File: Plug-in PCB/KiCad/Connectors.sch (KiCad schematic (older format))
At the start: 6 parts, among them J2 Conn_01x01, J3 Conn_01x01, J4 Conn_01x01, J5 Conn_01x01, J6 Conn_01x01, J7 Conn_01x01

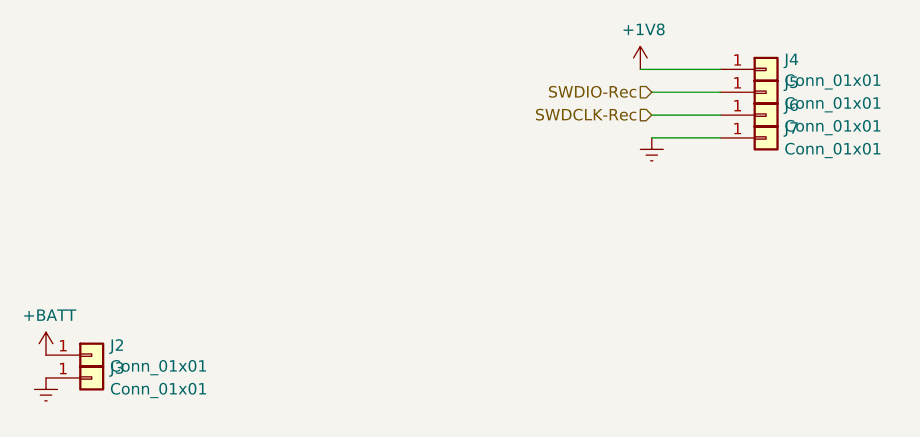
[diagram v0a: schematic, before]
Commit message: Wired Expansion Board Updates
1. KiCad: Schematics and layouts completed/Gerber files generated
2. Atmel: Communication protocol from WireFree to WiredExpansion written
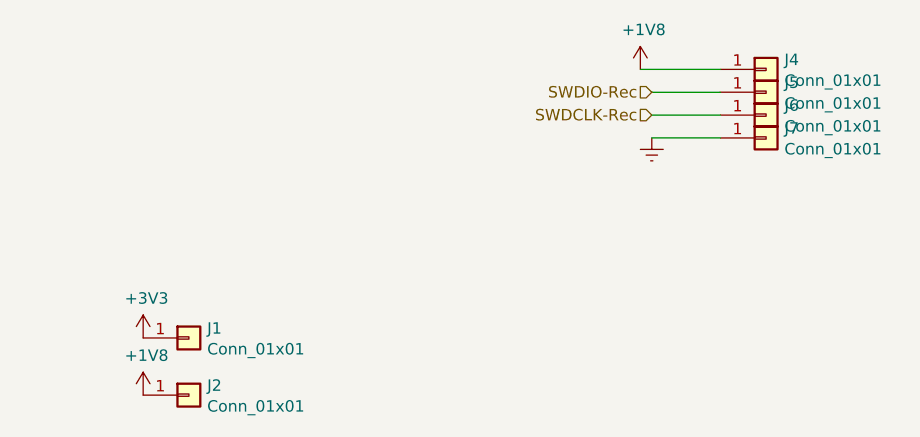
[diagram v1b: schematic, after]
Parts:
- removed J3: Conn_01x01, Connector_PinHeader_2.54mm:PinHeader_1x01_P2.54mm_Vertical, symbol .Connector:Conn_01x01
- added J1: Conn_01x01, Connector_PinHeader_2.54mm:PinHeader_1x01_P2.54mm_Vertical, symbol .Connector:Conn_01x01
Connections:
- net +BATT is gone; now on net +1V8: J2.1 (Pin_1)
- new net +3V3: J1.1 (Pin_1)
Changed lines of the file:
@@
 $EndDescr
-$Comp
-L .Connector:Conn_01x01 J2
-U 1 1 5CA26767
-P 4450 4100
-F 0 "J2" H 4530 4142 50  0000 L CNN
-F 1 "Conn_01x01" H 4530 4051 50  0000 L CNN
-F 2 "Connector_PinHeader_2.54mm:PinHeader_1x01_P2.54mm_Vertical" H 4450 4100 50  0001 C CNN
-F 3 "~" H 4450 4100 50  0001 C CNN
-	1    4450 4100
-	1    0    0    -1
-$EndComp
-$Comp
-L .Connector:Conn_01x01 J3
-U 1 1 5CA267B7
-P 4450 4200
-F 0 "J3" H 4530 4242 50  0000 L CNN
-F 1 "Conn_01x01" H 4530 4151 50  0000 L CNN
-F 2 "Connector_PinHeader_2.54mm:PinHeader_1x01_P2.54mm_Vertical" H 4450 4200 50  0001 C CNN
-F 3 "~" H 4450 4200 50  0001 C CNN
-	1    4450 4200
-	1    0    0    -1
-$EndComp
-$Comp
-L power:+BATT #PWR032
-U 1 1 5CA268F4
-P 4250 4100
-F 0 "#PWR032" H 4250 3950 50  0001 C CNN
-F 1 "+BATT" H 4265 4273 50  0000 C CNN
-F 2 "" H 4250 4100 50  0001 C CNN
-F 3 "" H 4250 4100 50  0001 C CNN
-	1    4250 4100
-	1    0    0    -1
-$EndComp
-$Comp
-L power:Earth #PWR033
-U 1 1 5CA26FF1
-P 4250 4200
-F 0 "#PWR033" H 4250 3950 50  0001 C CNN
-F 1 "Earth" H 4250 4050 50  0001 C CNN
-F 2 "" H 4250 4200 50  0001 C CNN
-F 3 "~" H 4250 4200 50  0001 C CNN
-	1    4250 4200
-	1    0    0    -1
-$EndComp
 $Comp
 L power:+1V8 #PWR034
@@
 Text HLabel 6900 2950 0    50   Input ~ 0
 SWDIO-Rec
+$Comp
+L power:+3V3 #PWR01
+U 1 1 5D5EEA1B
+P 4675 4025
+F 0 "#PWR01" H 4675 3875 50  0001 C CNN
+F 1 "+3V3" H 4690 4198 50  0000 C CNN
+F 2 "" H 4675 4025 50  0001 C CNN
+F 3 "" H 4675 4025 50  0001 C CNN
+	1    4675 4025
+	1    0    0    -1
+$EndComp
+$Comp
+L power:+1V8 #PWR02
+U 1 1 5D5EEDA1
+P 4675 4275
+F 0 "#PWR02" H 4675 4125 50  0001 C CNN
+F 1 "+1V8" H 4690 4448 50  0000 C CNN
+F 2 "" H 4675 4275 50  0001 C CNN
+F 3 "" H 4675 4275 50  0001 C CNN
+	1    4675 4275
+	1    0    0    -1
+$EndComp
+$Comp
+L .Connector:Conn_01x01 J1
+U 1 1 5D5EF97F
+P 4875 4025
+F 0 "J1" H 4955 4067 50  0000 L CNN
+F 1 "Conn_01x01" H 4955 3976 50  0000 L CNN
+F 2 "Connector_PinHeader_2.54mm:PinHeader_1x01_P2.54mm_Vertical" H 4875 4025 50  0001 C CNN
+F 3 "~" H 4875 4025 50  0001 C CNN
+	1    4875 4025
+	1    0    0    -1
+$EndComp
+$Comp
+L .Connector:Conn_01x01 J2
+U 1 1 5D5F04EA
+P 4875 4275
+F 0 "J2" H 4955 4317 50  0000 L CNN
+F 1 "Conn_01x01" H 4955 4226 50  0000 L CNN
+F 2 "Connector_PinHeader_2.54mm:PinHeader_1x01_P2.54mm_Vertical" H 4875 4275 50  0001 C CNN
+F 3 "~" H 4875 4275 50  0001 C CNN
+	1    4875 4275
+	1    0    0    -1
+$EndComp
 $EndSCHEMATC

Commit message: Change MCU and Serializer Power to 3.3V
1. MCU VDDIO, SWD, VDDIN, VDDUTMII powered at 3.3V

2. Serializer VDDIO, PDB powered at 3.3V

3. Layout changed (Pins enlarged, Coax_Gnd added, Coax connector moved closer to seralizer)
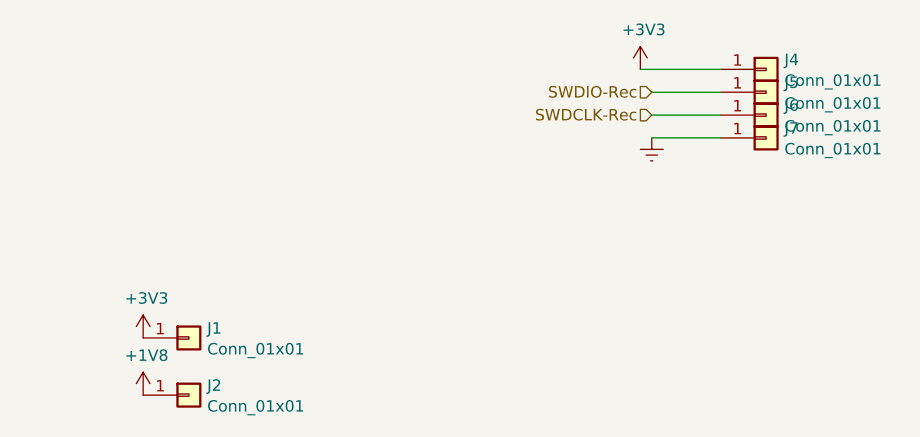
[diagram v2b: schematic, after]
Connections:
- net +1V8: no longer J4.1 (Pin_1)
- net +3V3: now also J4.1 (Pin_1)
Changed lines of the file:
@@
 $EndDescr
-$Comp
-L power:+1V8 #PWR034
-U 1 1 5CC8E5DF
-P 6850 2850
-F 0 "#PWR034" H 6850 2700 50  0001 C CNN
-F 1 "+1V8" H 6865 3023 50  0000 C CNN
-F 2 "" H 6850 2850 50  0001 C CNN
-F 3 "" H 6850 2850 50  0001 C CNN
-	1    6850 2850
-	1    0    0    -1
-$EndComp
 $Comp
 L power:Earth #PWR035
@@
 	1    0    0    -1
 $EndComp
+$Comp
+L power:+3V3 #PWR0128
+U 1 1 5D68DC19
+P 6850 2850
+F 0 "#PWR0128" H 6850 2700 50  0001 C CNN
+F 1 "+3V3" H 6865 3023 50  0000 C CNN
+F 2 "" H 6850 2850 50  0001 C CNN
+F 3 "" H 6850 2850 50  0001 C CNN
+	1    6850 2850
+	1    0    0    -1
+$EndComp
